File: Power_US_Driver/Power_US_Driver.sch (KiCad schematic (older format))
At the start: 11 parts

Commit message: quick sketch of referenc implementation.
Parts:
- removed R?: R, symbol R
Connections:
- net labels added: GND
- wire segments 4 -> 21
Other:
- note added: "Coax jacket connects to case. should be GND"
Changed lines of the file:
@@
 	-1   0    0    -1
 $EndComp
-Wire Wire Line
-	5150 2850 5400 2850
-Wire Wire Line
-	5400 2850 5400 3300
-Wire Wire Line
-	5600 3150 5600 2850
-Wire Wire Line
-	5600 2850 6150 2850
 $Comp
 L R R?
@@
 $Comp
 L R R?
-U 1 1 5AAD7D40
-P 6350 2100
-F 0 "R?" V 6430 2100 50  0000 C CNN
-F 1 "R" V 6350 2100 50  0000 C CNN
-F 2 "" V 6280 2100 50  0001 C CNN
-F 3 "" H 6350 2100 50  0001 C CNN
-	1    6350 2100
-	0    1    1    0
-$EndComp
-$Comp
-L R R?
 U 1 1 5AAD7D77
 P 6350 2350
@@
 	1    0    0    -1
 $EndComp
+$Comp
+L GND #PWR?
+U 1 1 5AAD816F
+P 4250 3350
+F 0 "#PWR?" H 4250 3100 50  0001 C CNN
+F 1 "GND" H 4250 3200 50  0000 C CNN
+F 2 "" H 4250 3350 50  0001 C CNN
+F 3 "" H 4250 3350 50  0001 C CNN
+	1    4250 3350
+	1    0    0    -1
+$EndComp
+$Comp
+L GND #PWR?
+U 1 1 5AAD8197
+P 6800 3500
+F 0 "#PWR?" H 6800 3250 50  0001 C CNN
+F 1 "GND" H 6800 3350 50  0000 C CNN
+F 2 "" H 6800 3500 50  0001 C CNN
+F 3 "" H 6800 3500 50  0001 C CNN
+	1    6800 3500
+	1    0    0    -1
+$EndComp
+$Comp
+L GND #PWR?
+U 1 1 5AAD81BF
+P 7100 3500
+F 0 "#PWR?" H 7100 3250 50  0001 C CNN
+F 1 "GND" H 7100 3350 50  0000 C CNN
+F 2 "" H 7100 3500 50  0001 C CNN
+F 3 "" H 7100 3500 50  0001 C CNN
+	1    7100 3500
+	1    0    0    -1
+$EndComp
+Wire Wire Line
+	5400 2850 5150 2850
+Wire Wire Line
+	5400 2100 5400 3300
+Wire Wire Line
+	5600 2350 5600 3150
+Wire Wire Line
+	5600 2850 6150 2850
+Wire Wire Line
+	4400 2100 4700 2100
+Wire Wire Line
+	4950 2600 4950 2700
+Wire Wire Line
+	5250 2600 5400 2600
+Connection ~ 5400 2850
+Wire Wire Line
+	5900 2600 6350 2600
+Wire Wire Line
+	6350 2600 6350 2700
+Wire Wire Line
+	5000 2100 5700 2100
+Connection ~ 5600 2600
+Connection ~ 5400 2600
+Wire Wire Line
+	4550 2950 4400 2950
+Wire Wire Line
+	4400 2950 4400 2100
+Wire Wire Line
+	6900 2950 6750 2950
+Wire Wire Line
+	6900 2100 6900 2950
+Wire Wire Line
+	6900 2350 6500 2350
+Connection ~ 6900 2350
+Wire Wire Line
+	6000 2100 6900 2100
+Wire Wire Line
+	6200 2350 5600 2350
+Connection ~ 5600 2350
+Connection ~ 5400 2100
+Wire Wire Line
+	4250 3350 4250 2750
+Wire Wire Line
+	4250 2750 4550 2750
+Wire Wire Line
+	6750 2750 6800 2750
+Wire Wire Line
+	6800 2750 6800 3500
+Text Notes 4850 4000 0    60   ~ 0
+Coax jacket connects to case. should be GND
 $EndSCHEMATC

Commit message: created hiarchical sheets, started sketching major comps.
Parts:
- removed J?: Conn_Coaxial, symbol Conn_Coaxial
- removed R? (x7): R, symbol R
- removed U? (x2): PA341, Housings_SSOP:MSOP-8-1EP_3x3mm_Pitch0.65mm, symbol PA341
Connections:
- net labels removed: GND
- wire segments 21 -> 0
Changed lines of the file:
@@
 $Descr A4 11693 8268
 encoding utf-8
-Sheet 1 1
+Sheet 1 5
 Title ""
 Date ""
@@
 Comment4 ""
 $EndDescr
-$Comp
-L Conn_Coaxial J?
-U 1 1 5AAD3631
-P 5600 3300
-F 0 "J?" H 5610 3420 50  0000 C CNN
-F 1 "Conn_Coaxial" V 5715 3300 50  0000 C CNN
-F 2 "" H 5600 3300 50  0001 C CNN
-F 3 "" H 5600 3300 50  0001 C CNN
-	1    5600 3300
-	0    1    1    0
-$EndComp
-$Comp
-L PA341 U?
-U 1 1 5AAD7B98
-P 4850 2850
-F 0 "U?" H 4550 3100 50  0000 L CNN
-F 1 "PA341" H 4650 2850 50  0000 L CNN
-F 2 "Housings_SSOP:MSOP-8-1EP_3x3mm_Pitch0.65mm" H 4950 2300 50  0001 C CNN
-F 3 "" H 4850 3050 50  0001 C CNN
-	1    4850 2850
-	1    0    0    -1
-$EndComp
-$Comp
-L PA341 U?
-U 1 1 5AAD7BC9
-P 6450 2850
-F 0 "U?" H 6150 3100 50  0000 L CNN
-F 1 "PA341" H 6250 2850 50  0000 L CNN
-F 2 "Housings_SSOP:MSOP-8-1EP_3x3mm_Pitch0.65mm" H 6550 2300 50  0001 C CNN
-F 3 "" H 6450 3050 50  0001 C CNN
-	1    6450 2850
-	-1   0    0    -1
-$EndComp
-$Comp
-L R R?
-U 1 1 5AAD7C3B
-P 5100 2600
-F 0 "R?" V 5180 2600 50  0000 C CNN
-F 1 "R" V 5100 2600 50  0000 C CNN
-F 2 "" V 5030 2600 50  0001 C CNN
-F 3 "" H 5100 2600 50  0001 C CNN
-	1    5100 2600
-	0    1    1    0
-$EndComp
-$Comp
-L R R?
-U 1 1 5AAD7C76
-P 5750 2600
-F 0 "R?" V 5830 2600 50  0000 C CNN
-F 1 "R" V 5750 2600 50  0000 C CNN
-F 2 "" V 5680 2600 50  0001 C CNN
-F 3 "" H 5750 2600 50  0001 C CNN
-	1    5750 2600
-	0    1    1    0
-$EndComp
-$Comp
-L R R?
-U 1 1 5AAD7CA3
-P 4250 2100
-F 0 "R?" V 4330 2100 50  0000 C CNN
-F 1 "R" V 4250 2100 50  0000 C CNN
-F 2 "" V 4180 2100 50  0001 C CNN
-F 3 "" H 4250 2100 50  0001 C CNN
-	1    4250 2100
-	0    1    1    0
-$EndComp
-$Comp
-L R R?
-U 1 1 5AAD7CE2
-P 4850 2100
-F 0 "R?" V 4930 2100 50  0000 C CNN
-F 1 "R" V 4850 2100 50  0000 C CNN
-F 2 "" V 4780 2100 50  0001 C CNN
-F 3 "" H 4850 2100 50  0001 C CNN
-	1    4850 2100
-	0    1    1    0
-$EndComp
-$Comp
-L R R?
-U 1 1 5AAD7D11
-P 5850 2100
-F 0 "R?" V 5930 2100 50  0000 C CNN
-F 1 "R" V 5850 2100 50  0000 C CNN
-F 2 "" V 5780 2100 50  0001 C CNN
-F 3 "" H 5850 2100 50  0001 C CNN
-	1    5850 2100
-	0    1    1    0
-$EndComp
-$Comp
-L R R?
-U 1 1 5AAD7D77
-P 6350 2350
-F 0 "R?" V 6430 2350 50  0000 C CNN
-F 1 "R" V 6350 2350 50  0000 C CNN
-F 2 "" V 6280 2350 50  0001 C CNN
-F 3 "" H 6350 2350 50  0001 C CNN
-	1    6350 2350
-	0    1    1    0
-$EndComp
-$Comp
-L R R?
-U 1 1 5AAD7DAC
-P 7100 3150
-F 0 "R?" V 7180 3150 50  0000 C CNN
-F 1 "R" V 7100 3150 50  0000 C CNN
-F 2 "" V 7030 3150 50  0001 C CNN
-F 3 "" H 7100 3150 50  0001 C CNN
-	1    7100 3150
-	1    0    0    -1
-$EndComp
-$Comp
-L GND #PWR?
-U 1 1 5AAD816F
-P 4250 3350
-F 0 "#PWR?" H 4250 3100 50  0001 C CNN
-F 1 "GND" H 4250 3200 50  0000 C CNN
-F 2 "" H 4250 3350 50  0001 C CNN
-F 3 "" H 4250 3350 50  0001 C CNN
-	1    4250 3350
-	1    0    0    -1
-$EndComp
-$Comp
-L GND #PWR?
-U 1 1 5AAD8197
-P 6800 3500
-F 0 "#PWR?" H 6800 3250 50  0001 C CNN
-F 1 "GND" H 6800 3350 50  0000 C CNN
-F 2 "" H 6800 3500 50  0001 C CNN
-F 3 "" H 6800 3500 50  0001 C CNN
-	1    6800 3500
-	1    0    0    -1
-$EndComp
-$Comp
-L GND #PWR?
-U 1 1 5AAD81BF
-P 7100 3500
-F 0 "#PWR?" H 7100 3250 50  0001 C CNN
-F 1 "GND" H 7100 3350 50  0000 C CNN
-F 2 "" H 7100 3500 50  0001 C CNN
-F 3 "" H 7100 3500 50  0001 C CNN
-	1    7100 3500
-	1    0    0    -1
-$EndComp
-Wire Wire Line
-	5400 2850 5150 2850
-Wire Wire Line
-	5400 2100 5400 3300
-Wire Wire Line
-	5600 2350 5600 3150
-Wire Wire Line
-	5600 2850 6150 2850
-Wire Wire Line
-	4400 2100 4700 2100
-Wire Wire Line
-	4950 2600 4950 2700
-Wire Wire Line
-	5250 2600 5400 2600
-Connection ~ 5400 2850
-Wire Wire Line
-	5900 2600 6350 2600
-Wire Wire Line
-	6350 2600 6350 2700
-Wire Wire Line
-	5000 2100 5700 2100
-Connection ~ 5600 2600
-Connection ~ 5400 2600
-Wire Wire Line
-	4550 2950 4400 2950
-Wire Wire Line
-	4400 2950 4400 2100
-Wire Wire Line
-	6900 2950 6750 2950
-Wire Wire Line
-	6900 2100 6900 2950
-Wire Wire Line
-	6900 2350 6500 2350
-Connection ~ 6900 2350
-Wire Wire Line
-	6000 2100 6900 2100
-Wire Wire Line
-	6200 2350 5600 2350
-Connection ~ 5600 2350
-Connection ~ 5400 2100
-Wire Wire Line
-	4250 3350 4250 2750
-Wire Wire Line
-	4250 2750 4550 2750
-Wire Wire Line
-	6750 2750 6800 2750
-Wire Wire Line
-	6800 2750 6800 3500
 Text Notes 4850 4000 0    60   ~ 0
 Coax jacket connects to case. should be GND
+$Sheet
+S 7400 2350 1050 1300
+U 5AAD8D83
+F0 "Power_Supply" 60
+F1 "Power_Supply.sch" 60
+F2 "V+" O R 8450 2600 60
+F3 "V-" O R 8450 2900 60
+F4 "HOT" I L 7400 2450 60
+F5 "Nuetral" I L 7400 2750 60
+F6 "CHASSIS_GND" I L 7400 3100 60
+F7 "12v" O R 8450 3200 60
+F8 "3v3" O R 8450 3500 60
+$EndSheet
+$Sheet
+S 7500 4500 650  1050
+U 5AAD8FE6
+F0 "DDS" 60
+F1 "DDS.sch" 60
+$EndSheet
+$Sheet
+S 5350 4550 650  1050
+U 5AAD908C
+F0 "phase_comp" 60
+F1 "phase_comp.sch" 60
+$EndSheet
+$Sheet
+S 3850 4600 700  1050
+U 5AAD9099
+F0 "power_amp" 60
+F1 "power_amp.sch" 60
+F2 "Sig_Out" O R 4550 5000 60
+F3 "Sig_in" I L 3850 5100 60
+F4 "v+" I L 3850 4750 60
+F5 "v-" I L 3850 5400 60
+F6 "Vref" I L 3850 5250 60
+$EndSheet
 $EndSCHEMATC

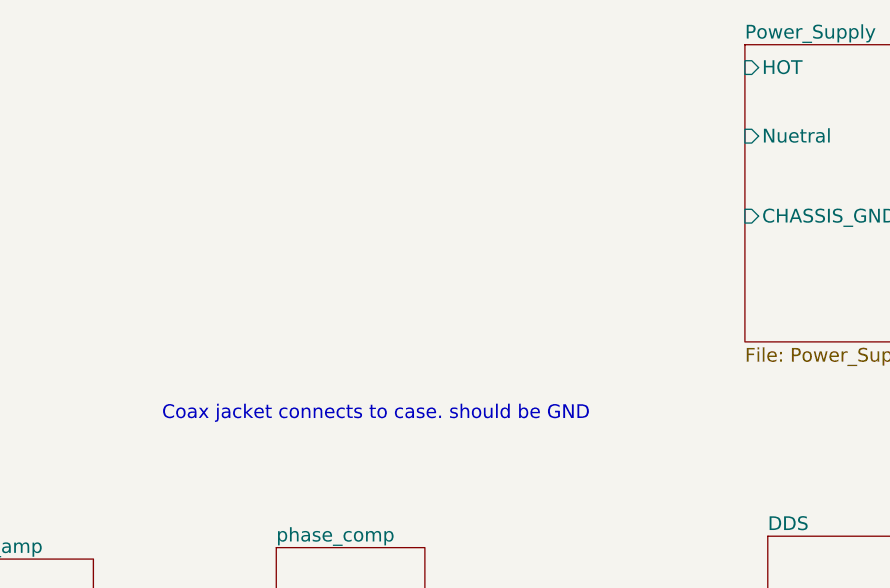
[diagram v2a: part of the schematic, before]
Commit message: Abandoned Op amp solution for power FEt producing square wave solution.
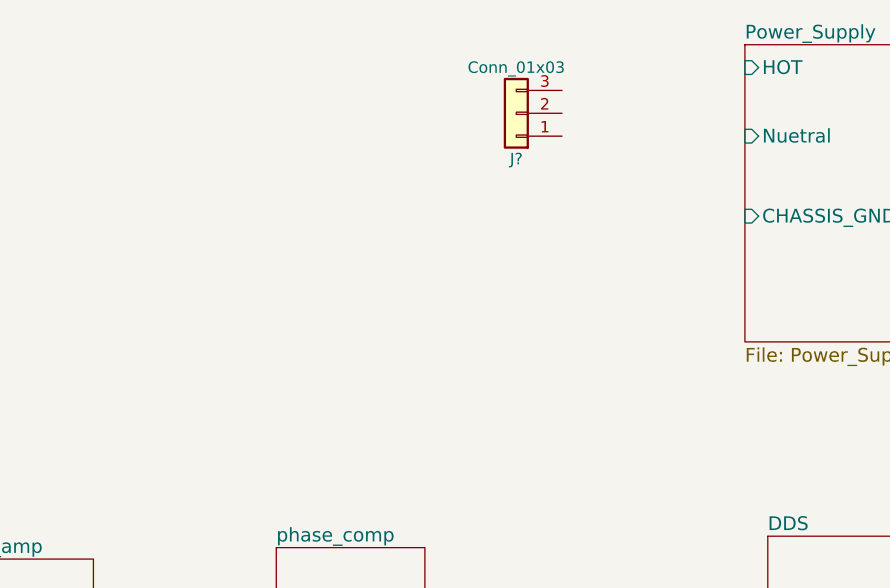
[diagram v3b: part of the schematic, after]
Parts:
- added J?: Conn_01x03, symbol Conn_01x03
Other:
- note removed: "Coax jacket connects to case. should be GND"
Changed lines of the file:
@@
 Comment4 ""
 $EndDescr
-Text Notes 4850 4000 0    60   ~ 0
-Coax jacket connects to case. should be GND
 $Sheet
 S 7400 2350 1050 1300
@@
 F6 "Vref" I L 3850 5250 60
 $EndSheet
+$Comp
+L Conn_01x03 J?
+U 1 1 5AAE7F4F
+P 6400 2650
+F 0 "J?" H 6400 2850 50  0000 C CNN
+F 1 "Conn_01x03" H 6400 2450 50  0000 C CNN
+F 2 "" H 6400 2650 50  0001 C CNN
+F 3 "" H 6400 2650 50  0001 C CNN
+	1    6400 2650
+	-1   0    0    1
+$EndComp
 $EndSCHEMATC

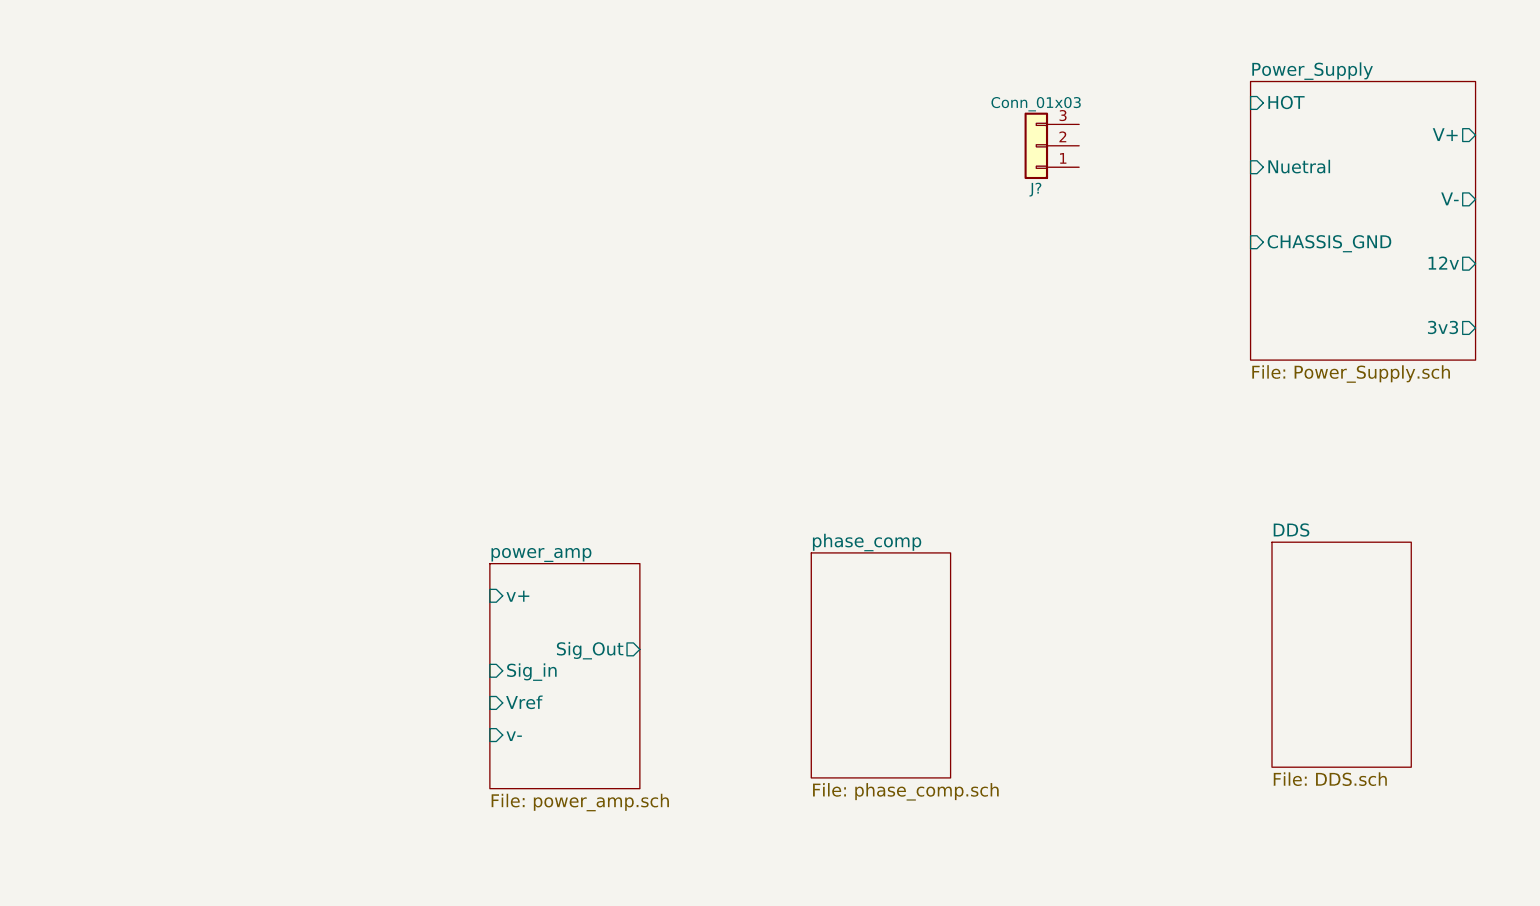
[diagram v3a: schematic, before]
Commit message: added fet driver and DDS module connection
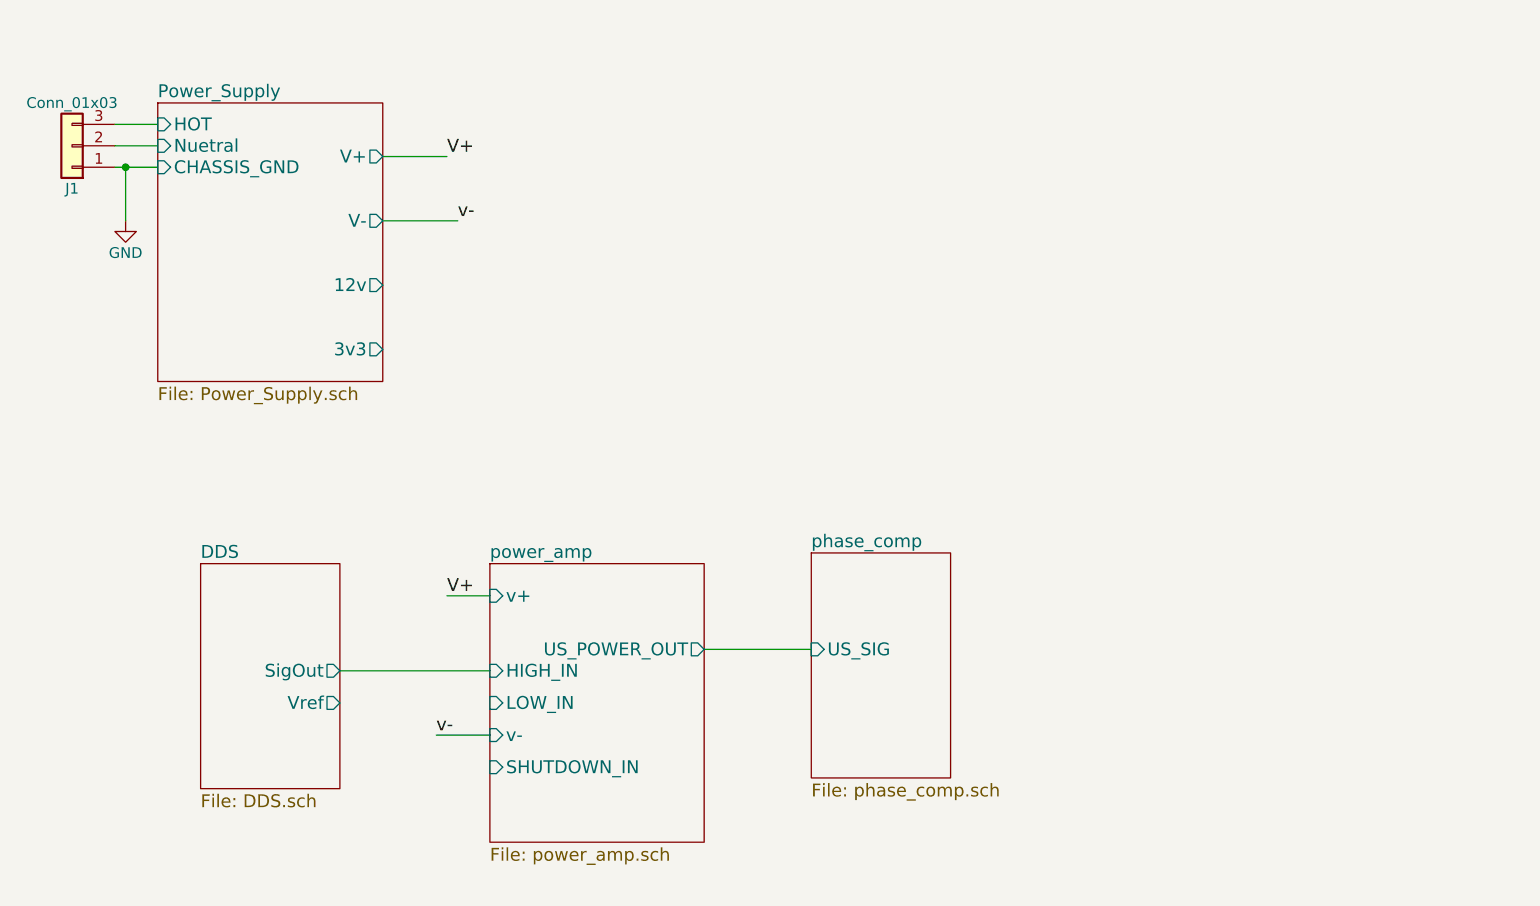
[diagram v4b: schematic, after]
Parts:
- gave numbers to parts that had none: 1
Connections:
- net Power_Supply/HOT: now also J1.3 (Pin_3)
- net Power_Supply/Nuetral: now also J1.2 (Pin_2)
- net GND: now reaches J1.1 (Pin_1)
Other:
- moved on the sheet: J1
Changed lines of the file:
@@
 $EndDescr
 $Sheet
-S 7400 2350 1050 1300
+S 2300 2450 1050 1300
 U 5AAD8D83
 F0 "Power_Supply" 60
 F1 "Power_Supply.sch" 60
-F2 "V+" O R 8450 2600 60
-F3 "V-" O R 8450 2900 60
-F4 "HOT" I L 7400 2450 60
-F5 "Nuetral" I L 7400 2750 60
-F6 "CHASSIS_GND" I L 7400 3100 60
-F7 "12v" O R 8450 3200 60
-F8 "3v3" O R 8450 3500 60
+F2 "V+" O R 3350 2700 60
+F3 "V-" O R 3350 3000 60
+F4 "HOT" I L 2300 2550 60
+F5 "Nuetral" I L 2300 2650 60
+F6 "CHASSIS_GND" I L 2300 2750 60
+F7 "12v" O R 3350 3300 60
+F8 "3v3" O R 3350 3600 60
 $EndSheet
 $Sheet
-S 7500 4500 650  1050
+S 2500 4600 650  1050
 U 5AAD8FE6
 F0 "DDS" 60
 F1 "DDS.sch" 60
+F2 "SigOut" O R 3150 5100 60
+F3 "Vref" O R 3150 5250 60
 $EndSheet
 $Sheet
@@
 F0 "phase_comp" 60
 F1 "phase_comp.sch" 60
+F2 "US_SIG" I L 5350 5000 60
 $EndSheet
 $Sheet
-S 3850 4600 700  1050
+S 3850 4600 1000 1300
 U 5AAD9099
 F0 "power_amp" 60
 F1 "power_amp.sch" 60
-F2 "Sig_Out" O R 4550 5000 60
-F3 "Sig_in" I L 3850 5100 60
-F4 "v+" I L 3850 4750 60
-F5 "v-" I L 3850 5400 60
-F6 "Vref" I L 3850 5250 60
+F2 "v+" I L 3850 4750 60
+F3 "v-" I L 3850 5400 60
+F4 "US_POWER_OUT" O R 4850 5000 60
+F5 "HIGH_IN" I L 3850 5100 60
+F6 "LOW_IN" I L 3850 5250 60
+F7 "SHUTDOWN_IN" I L 3850 5550 60
 $EndSheet
 $Comp
-L Conn_01x03 J?
+L Conn_01x03 J1
 U 1 1 5AAE7F4F
-P 6400 2650
-F 0 "J?" H 6400 2850 50  0000 C CNN
-F 1 "Conn_01x03" H 6400 2450 50  0000 C CNN
-F 2 "" H 6400 2650 50  0001 C CNN
-F 3 "" H 6400 2650 50  0001 C CNN
-	1    6400 2650
+P 1900 2650
+F 0 "J1" H 1900 2850 50  0000 C CNN
+F 1 "Conn_01x03" H 1900 2450 50  0000 C CNN
+F 2 "" H 1900 2650 50  0001 C CNN
+F 3 "" H 1900 2650 50  0001 C CNN
+	1    1900 2650
 	-1   0    0    1
 $EndComp
+Wire Wire Line
+	3150 5100 3850 5100
+Text Label 3650 2700 0    60   ~ 0
+V+
+Text Label 3700 3000 0    60   ~ 0
+v-
+Wire Wire Line
+	3650 2700 3350 2700
+Text Label 3650 4750 0    60   ~ 0
+V+
+Wire Wire Line
+	3700 3000 3350 3000
+Text Label 3600 5400 0    60   ~ 0
+v-
+Wire Wire Line
+	3850 5400 3600 5400
+Wire Wire Line
+	3650 4750 3850 4750
+Wire Wire Line
+	2100 2550 2300 2550
+Wire Wire Line
+	2100 2650 2300 2650
+Wire Wire Line
+	2100 2750 2300 2750
+$Comp
+L GND #PWR1
+U 1 1 5AAE997E
+P 2150 3000
+F 0 "#PWR1" H 2150 2750 50  0001 C CNN
+F 1 "GND" H 2150 2850 50  0000 C CNN
+F 2 "" H 2150 3000 50  0001 C CNN
+F 3 "" H 2150 3000 50  0001 C CNN
+	1    2150 3000
+	1    0    0    -1
+$EndComp
+Wire Wire Line
+	2150 3000 2150 2750
+Connection ~ 2150 2750
+Wire Wire Line
+	5350 5000 4850 5000
 $EndSCHEMATC
